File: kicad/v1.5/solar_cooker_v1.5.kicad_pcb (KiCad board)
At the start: 2 copper layers, 88.9 x 99.1 mm, 9 parts, among them U1 microSD, U2 clock_module, U3 anemometer, U4 AM2315, U5 BME680, U6 PT100

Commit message: KiCad update
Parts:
- added D1: LED_GREEN, LED_SMD:LED_1206_3216Metric_Pad1.42x1.75mm_HandSolder, F.Cu at (210.8, 92.5)
- added D2: LED_RED, LED_SMD:LED_1206_3216Metric_Pad1.42x1.75mm_HandSolder, F.Cu at (218.4, 92.5)
- added S1: 500SSP1S2M2QEA, switch:SW_500SSP1S2M2QEA, F.Cu at (215.9, 70.7)
- added U7: pyranometer, custom_components:screw_terminal_4pin, F.Cu at (256.5, 104.1)
- R1: footprint Resistor_SMD:R_0201_0603Metric_Pad0.64x0.40mm_HandSolder -> Resistor_SMD:R_1206_3216Metric
- R2, R3: footprint Resistor_SMD:R_0201_0603Metric_Pad0.64x0.40mm_HandSolder -> Resistor_SMD:R_1206_3216Metric_Pad1.30x1.75mm_HandSolder
- moved R1 30.0 mm to (231.1, 99.1)
- moved R3 16.1 mm to (218.4, 84.0), turned to 90 degrees
- moved U5 15.2 mm to (200.7, 48.3)
- moved R2 14.2 mm to (210.8, 84.0), turned to 90 degrees
- moved U3 2.54 mm to (256.5, 83.8)
- moved U6 2.54 mm to (251.5, 38.1)

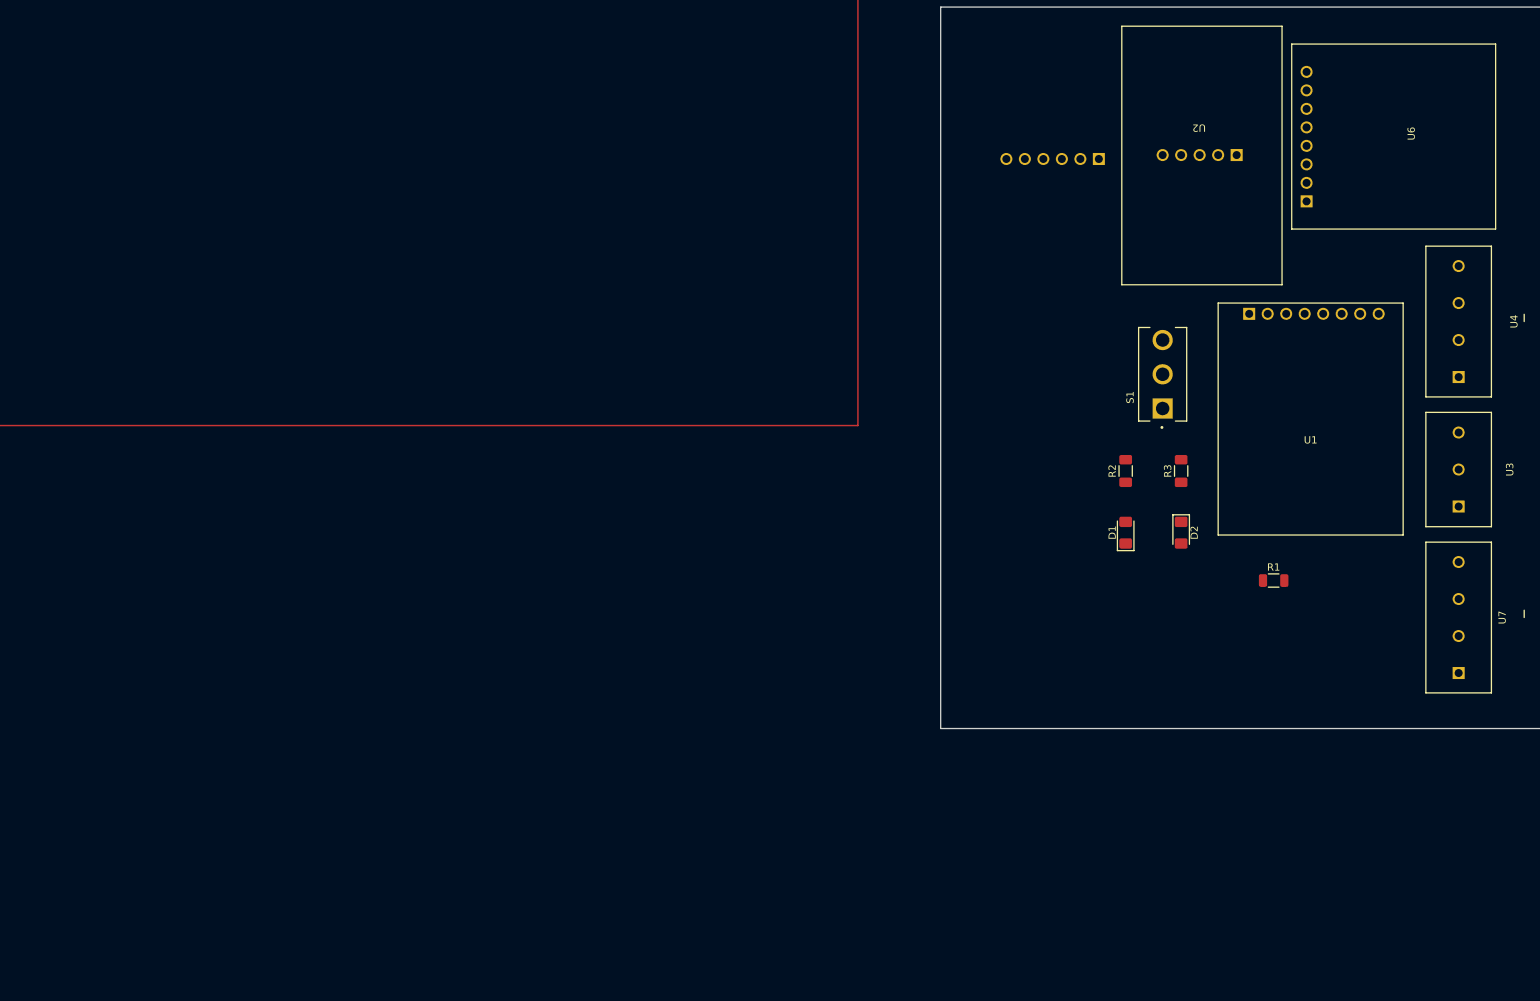
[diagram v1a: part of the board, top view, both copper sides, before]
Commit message: added Arduino Mega KiCad
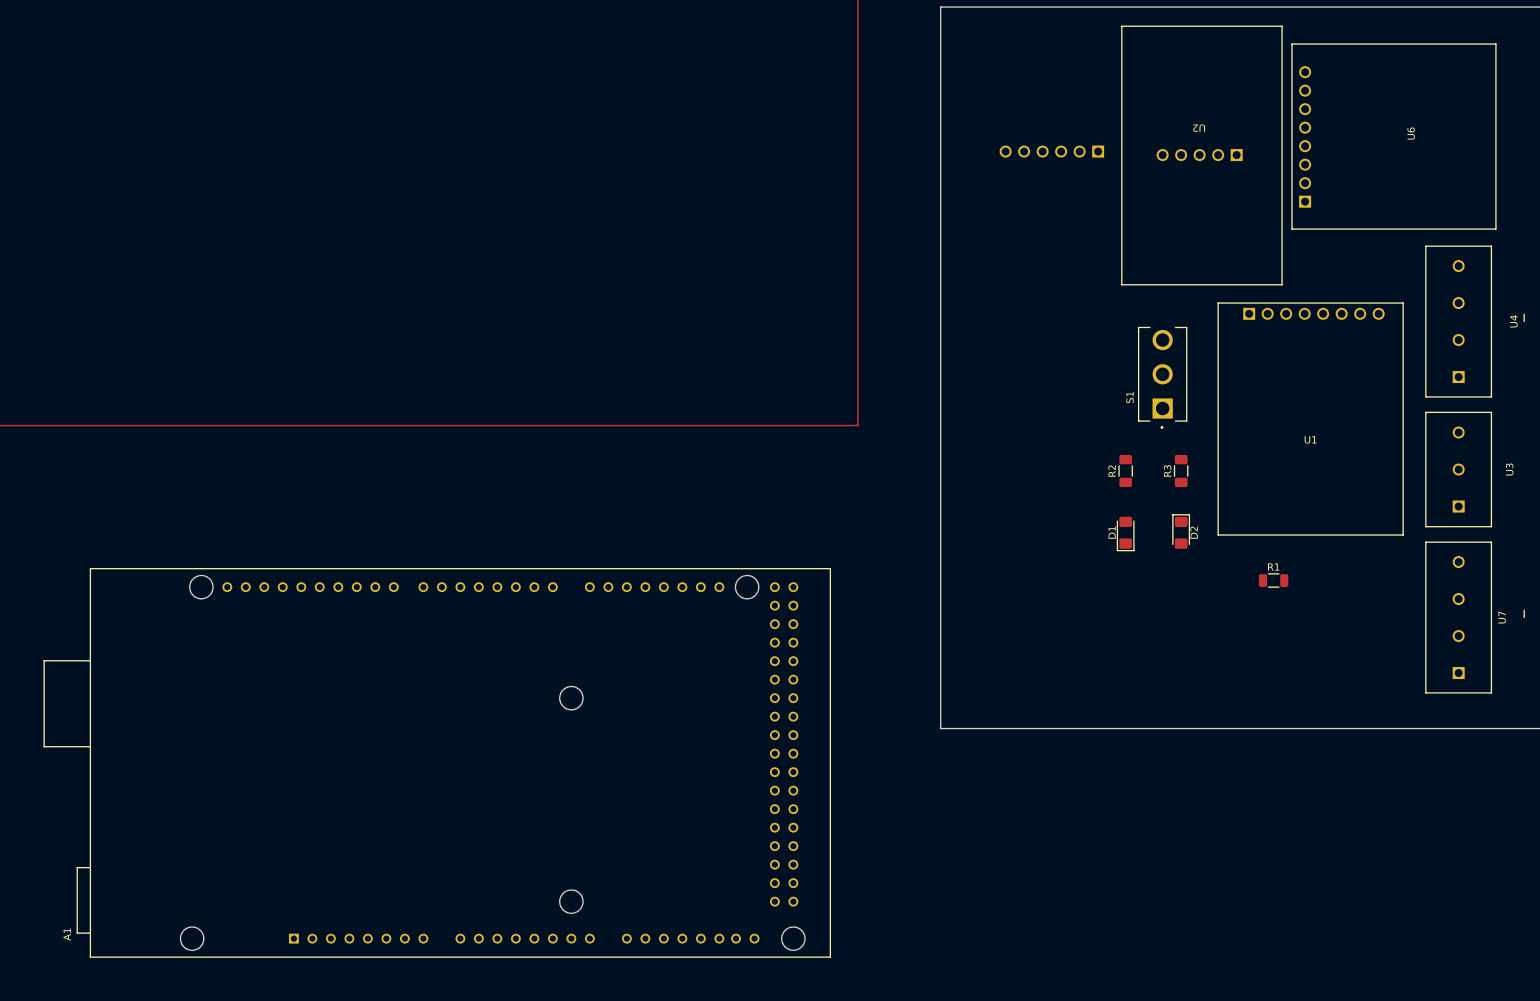
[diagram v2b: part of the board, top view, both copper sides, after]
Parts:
- added A1: A000067, Arduino Mega:ARDUINO_A000067, F.Cu at (119.5, 124.1)

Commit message: pcb has now 3 pt100 sensors
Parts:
- added U8: PT100, custom_components:PT100, F.Cu at (111.8, 147.8)
- added U9: PT100, custom_components:PT100, F.Cu at (80.1, 147.8)
- moved S1 199.1 mm to (33.0, 149.5)
- moved U1 198.6 mm to (43.2, 125.3), turned to -90 degrees
- moved U6 183.6 mm to (80.1, 103.9), turned to 0 degrees
- moved U2 182.9 mm to (46.8, 96.8), turned to 90 degrees
- moved U5 181.1 mm to (50.8, 149.9), turned to 90 degrees
- moved U7 123.1 mm to (142.2, 149.9), turned to 0 degrees
- moved U3 114.9 mm to (162.6, 149.9), turned to 0 degrees
- moved U4 113.5 mm to (182.9, 149.9), turned to 0 degrees
- moved R3 71.5 mm to (209.3, 154.9), turned to 0 degrees
- moved D2 64.9 mm to (200.8, 154.9), turned to 180 degrees
- moved A1 64.4 mm to (182.9, 113.0), turned to -90 degrees
- moved R2 63.3 mm to (209.3, 147.3), turned to 0 degrees
- moved D1 55.7 mm to (200.8, 147.3), turned to 0 degrees
- moved R1 53.4 mm to (218.4, 150.9), turned to -90 degrees
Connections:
- A1 pad 11: unconnected-(A1-Pad11) -> /D11
- A1 pad 20: unconnected-(A1-Pad20) -> /SDA
- A1 pad 21: unconnected-(A1-Pad21) -> /SCL
- A1 pad 22: unconnected-(A1-Pad22) -> /D22
- A1 pad 23: unconnected-(A1-Pad23) -> /D23
- A1 pad 24: unconnected-(A1-Pad24) -> /D24
- A1 pad 3: unconnected-(A1-Pad3) -> /D4
- A1 pad 50: unconnected-(A1-Pad50) -> /MISO
- A1 pad 51: unconnected-(A1-Pad51) -> /MOSI
- A1 pad 52: unconnected-(A1-Pad52) -> /SCK
- A1 pad 5V_1: unconnected-(A1-+5V_1-Pad5V_1) -> +5V
- A1 pad 6: unconnected-(A1-Pad6) -> /D6
- A1 pad AD0: unconnected-(A1-PadAD0) -> /A0
- A1 pad AD10: unconnected-(A1-PadAD10) -> /A10
- A1 pad GND1: unconnected-(A1-PadGND1) -> GND
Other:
- board size 88.9 x 99.1 mm -> 199.8 x 78.7 mm

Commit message: added GPS to pcb
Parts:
- added U10: GPS, custom_components:GPS, F.Cu at (93.8, 105.4)
- U5: moved to F.Cu
- moved S1 97.7 mm to (130.7, 147.5), turned to 180 degrees
- moved R3 94.4 mm to (116.5, 137.4), turned to 180 degrees
- moved R2 94.0 mm to (116.5, 131.9), turned to 180 degrees
- moved R1 90.2 mm to (128.3, 154.9), turned to 0 degrees
- moved U1 80.3 mm to (121.9, 109.2), turned to 180 degrees
- moved D2 80.1 mm to (122.6, 137.4), turned to 0 degrees
- moved D1 79.7 mm to (122.6, 131.9)
- moved U2 64.6 mm to (92.5, 142.5), turned to 0 degrees
- moved U5 63.1 mm to (113.9, 151.0), turned to 0 degrees
- moved U8 58.0 mm to (60.7, 120.3), turned to -90 degrees
- moved U6 22.4 mm to (60.5, 93.0), turned to -90 degrees
- moved U9 19.1 mm to (61.0, 147.6), turned to -90 degrees
- moved U4 11.7 mm to (194.4, 147.5)
- moved U3 11.3 mm to (173.6, 147.5)
- moved U7 10.8 mm to (152.8, 147.5)
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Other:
- board size 199.8 x 78.7 mm -> 155.4 x 77.1 mm
- board text added: "OFF"
- board text added: "ON"
- board text added: "SD card"
- board text added: "bottom of box"
- board text added: "entry cables"
- board text added: "external kabels"
- board text added: "powerbank"
- board text added: "top side of the box"

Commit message: routing update
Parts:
- moved R3 7.82 mm to (108.7, 137.1)
- moved R2 7.81 mm to (108.7, 132.1)
- moved D2 7.81 mm to (114.8, 137.1)
- moved D1 7.80 mm to (114.8, 132.1)
- moved R1 1.53 mm to (126.8, 154.8)
- moved U6 1.35 mm to (61.0, 94.3)
- moved U8 0.56 mm to (61.0, 120.8)
- moved U9 0.28 mm to (61.0, 147.3)
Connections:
- A1 pad 12: unconnected-(A1-Pad12) -> /D12
- A1 pad 13: unconnected-(A1-Pad13) -> /D13
- U6 pad 1: /White -> unconnected-(U6-RDY-Pad1)
- U6 pad 2: /White -> /D11
- U6 pad 3: /Red -> /MOSI
- U6 pad 4: /Red -> /MISO
- U6 pad 5: unconnected-(U6-RDY-Pad5) -> /SCK
- U6 pad 6: /D11 -> unconnected-(U6-3V3-Pad6)
- U6 pad 7: /MOSI -> GND
- U6 pad 8: /MISO -> +5V
- U8 pad 1: /White -> unconnected-(U8-RDY-Pad1)
- U8 pad 2: /White -> /D12
- U8 pad 3: /Red -> /MOSI
- U8 pad 4: /Red -> /MISO
- U8 pad 5: unconnected-(U8-RDY-Pad5) -> /SCK
- U8 pad 6: /D11 -> unconnected-(U8-3V3-Pad6)
- U8 pad 7: /MOSI -> GND
- U8 pad 8: /MISO -> +5V
- U9 pad 1: /White -> unconnected-(U9-RDY-Pad1)
- U9 pad 2: /White -> /D13
- U9 pad 3: /Red -> /MOSI
- U9 pad 4: /Red -> /MISO
- U9 pad 5: unconnected-(U9-RDY-Pad5) -> /SCK
- U9 pad 6: /D11 -> unconnected-(U9-3V3-Pad6)
- U9 pad 7: /MOSI -> GND
- U9 pad 8: /MISO -> +5V
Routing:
- net /SCK: track 0.00 -> 179.0 mm
- net /MISO: track 0.00 -> 157.4 mm
- net /MOSI: track 0.00 -> 155.9 mm
- net /D11: track 0.00 -> 148.1 mm
- net /D13: track 0.00 -> 148.1 mm
- net /D12: track 0.00 -> 140.9 mm
- net /SCL: track 0.00 -> 128.4 mm
- net /D6: track 0.00 -> 92.9 mm, vias 0 -> 1
- net /D4: track 0.00 -> 79.9 mm
- net /A10: track 0.00 -> 67.6 mm
- net +5V: track 0.00 -> 67.2 mm
- net /A0: track 0.00 -> 65.3 mm
- net /SDA: track 0.00 -> 42.9 mm
- net /D24: track 0.00 -> 34.5 mm

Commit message: routing update
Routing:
- net +5V: track 67.2 -> 220.7 mm, vias 0 -> 2
- net /SDA: track 42.9 -> 193.1 mm
- net /D22: track 0.00 -> 41.1 mm
- net /D23: track 0.00 -> 28.9 mm
- net Net-(D2-K): track 0.00 -> 3.08 mm
- net Net-(D1-K): track 0.00 -> 3.08 mm
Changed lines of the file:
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@@
     (effects (font (size 2 2) (thickness 0.3)) (justify left bottom))
   )
+  (segment (start 110.25 132.096429) (end 113.325 132.096429) (width 0.25) (layer "F.Cu") (net 1))
+  (segment (start 110.25 137.096428) (end 113.325 137.096428) (width 0.25) (layer "F.Cu") (net 3))
   (segment (start 186.9 128.3) (end 192.8 134.2) (width 0.25) (layer "F.Cu") (net 5))
   (segment (start 192.8 134.2) (end 192.8 135.7) (width 0.25) (layer "F.Cu") (net 5))
@@
   (segment (start 120.18 114.435933) (end 139.215933 95.4) (width 0.25) (layer "B.Cu") (net 8))
   (segment (start 139.215933 95.4) (end 144.46 95.4) (width 0.25) (layer "B.Cu") (net 8))
+  (segment (start 107.5446 146.4554) (end 106.68 147.32) (width 0.25) (layer "F.Cu") (net 10))
+  (segment (start 75.81 141.396346) (end 76.483654 142.07) (width 0.25) (layer "F.Cu") (net 10))
+  (segment (start 76.96 103.16) (end 75.81 104.31) (width 0.25) (layer "F.Cu") (net 10))
+  (segment (start 77.366346 142.24) (end 78.74 143.613654) (width 0.25) (layer "F.Cu") (net 10))
+  (segment (start 75.81 104.31) (end 75.81 114.896346) (width 0.25) (layer "F.Cu") (net 10))
+  (segment (start 91.3 143.76) (end 92.45 142.61) (width 0.25) (layer "F.Cu") (net 10))
+  (segment (start 83.65 142.07) (end 85.34 143.76) (width 0.25) (layer "F.Cu") (net 10))
+  (segment (start 75.81 114.896346) (end 76.483654 115.57) (width 0.25) (layer "F.Cu") (net 10))
+  (segment (start 76.96 129.66) (end 75.81 130.81) (width 0.25) (layer "F.Cu") (net 10))
+  (segment (start 78.74 127.88) (end 76.96 129.66) (width 0.25) (layer "F.Cu") (net 10))
+  (segment (start 85.34 143.76) (end 91.3 143.76) (width 0.25) (layer "F.Cu") (net 10))
+  (segment (start 106.1296 141.46) (end 107.5446 142.875) (width 0.25) (layer "F.Cu") (net 10))
+  (segment (start 78.74 143.613654) (end 78.74 147.32) (width 0.25) (layer "F.Cu") (net 10))
+  (segment (start 78.74 117.113654) (end 78.74 127.88) (width 0.25) (layer "F.Cu") (net 10))
+  (segment (start 93.6 141.46) (end 106.1296 141.46) (width 0.25) (layer "F.Cu") (net 10))
+  (segment (start 75.81 141.396346) (end 76.653654 142.24) (width 0.25) (layer "F.Cu") (net 10))
+  (segment (start 76.653654 142.24) (end 77.366346 142.24) (width 0.25) (layer "F.Cu") (net 10))
+  (segment (start 75.81 130.81) (end 75.81 141.396346) (width 0.25) (layer "F.Cu") (net 10))
+  (segment (start 92.45 142.61) (end 93.6 141.46) (width 0.25) (layer "F.Cu") (net 10))
+  (segment (start 107.5446 142.875) (end 107.5446 146.4554) (width 0.25) (layer "F.Cu") (net 10))
+  (segment (start 76.483654 142.07) (end 83.65 142.07) (width 0.25) (layer "F.Cu") (net 10))
+  (segment (start 77.196346 115.57) (end 78.74 117.113654) (width 0.25) (layer "F.Cu") (net 10))
+  (segment (start 76.483654 115.57) (end 77.196346 115.57) (width 0.25) (layer "F.Cu") (net 10))
+  (via (at 78.74 147.32) (size 0.8) (drill 0.4) (layers "F.Cu" "B.Cu") (net 10))
+  (via (at 106.68 147.32) (size 0.8) (drill 0.4) (layers "F.Cu" "B.Cu") (net 10))
   (segment (start 186.76 147.5) (end 195.58 138.68) (width 0.25) (layer "B.Cu") (net 10))
+  (segment (start 112.56 125.545) (end 112.56 137.86) (width 0.25) (layer "B.Cu") (net 10))
+  (segment (start 124.061396 141.725) (end 119.768254 141.725) (width 0.25) (layer "B.Cu") (net 10))
   (segment (start 195.58 138.68) (end 195.58 92.54) (width 0.25) (layer "B.Cu") (net 10))
+  (segment (start 78.74 154.38) (end 76.96 156.16) (width 0.25) (layer "B.Cu") (net 10))
+  (segment (start 128.85 146.513604) (end 124.061396 141.725) (width 0.25) (layer "B.Cu") (net 10))
+  (segment (start 128.85 148.313604) (end 128.85 146.513604) (width 0.25) (layer "B.Cu") (net 10))
+  (segment (start 129.786396 149.25) (end 128.85 148.313604) (width 0.25) (layer "B.Cu") (net 10))
+  (segment (start 119.0946 143.111346) (end 114.885946 147.32) (width 0.25) (layer "B.Cu") (net 10))
+  (segment (start 78.74 147.32) (end 78.74 154.38) (width 0.25) (layer "B.Cu") (net 10))
+  (segment (start 119.768254 141.725) (end 119.0946 142.398654) (width 0.25) (layer "B.Cu") (net 10))
+  (segment (start 107.545 142.875) (end 107.5446 142.875) (width 0.25) (layer "B.Cu") (net 10))
   (segment (start 195.58 92.54) (end 201.64 86.48) (width 0.25) (layer "B.Cu") (net 10))
+  (segment (start 112.56 137.86) (end 107.545 142.875) (width 0.25) (layer "B.Cu") (net 10))
+  (segment (start 119.0946 142.398654) (end 119.0946 143.111346) (width 0.25) (layer "B.Cu") (net 10))
+  (segment (start 135.4246 147.5) (end 133.6746 149.25) (width 0.25) (layer "B.Cu") (net 10))
+  (segment (start 111.76 147.32) (end 106.68 147.32) (width 0.25) (layer "B.Cu") (net 10))
+  (segment (start 133.6746 149.25) (end 129.786396 149.25) (width 0.25) (layer "B.Cu") (net 10))
+  (segment (start 114.885946 147.32) (end 111.76 147.32) (width 0.25) (layer "B.Cu") (net 10))
+  (segment (start 153.747604 93.096) (end 159.996 86.847604) (width 0.25) (layer "B.Cu") (net 11))
   (segment (start 178.4 149.6) (end 164.544 135.744) (width 0.25) (layer "B.Cu") (net 11))
+  (segment (start 87.37 142.61) (end 136.884 93.096) (width 0.25) (layer "B.Cu") (net 11))
   (segment (start 164.544 135.744) (end 156.924 135.744) (width 0.25) (layer "B.Cu") (net 11))
+  (segment (start 160.584129 85.476) (end 161.415871 85.476) (width 0.25) (layer "B.Cu") (net 11))
+  (segment (start 161.415871 85.476) (end 162.004 86.064129) (width 0.25) (layer "B.Cu") (net 11))
   (segment (start 156.924 135.744) (end 155.92 134.74) (width 0.25) (layer "B.Cu") (net 11))
+  (segment (start 159.996 86.064129) (end 160.584129 85.476) (width 0.25) (layer "B.Cu") (net 11))
   (segment (start 191.84 147.5) (end 189.74 149.6) (width 0.25) (layer "B.Cu") (net 11))
+  (segment (start 159.996 86.847604) (end 159.996 86.064129) (width 0.25) (layer "B.Cu") (net 11))
   (segment (start 189.74 149.6) (end 178.4 149.6) (width 0.25) (layer "B.Cu") (net 11))
+  (segment (start 136.884 93.096) (end 153.747604 93.096) (width 0.25) (layer "B.Cu") (net 11))
+  (segment (start 162.004 86.064129) (end 162.004 128.656) (width 0.25) (layer "B.Cu") (net 11))
+  (segment (start 162.004 128.656) (end 155.92 134.74) (width 0.25) (layer "B.Cu") (net 11))
   (segment (start 126.6 126.6) (end 131 131) (width 0.25) (layer "F.Cu") (net 12))
   (segment (start 118.9 125) (end 119.7 124.2) (width 0.25) (layer "F.Cu") (net 12))
@@
   (segment (start 142.6 131) (end 144.42 131) (width 0.25) (layer "B.Cu") (net 17))
   (segment (start 144.42 131) (end 145.76 129.66) (width 0.25) (layer "B.Cu") (net 17))
+  (segment (start 115.498928 138.296428) (end 114.3625 137.16) (width 0.25) (layer "F.Cu") (net 18))
+  (segment (start 145.76 132.2) (end 144.224 133.736) (width 0.25) (layer "F.Cu") (net 18))
+  (segment (start 114.3625 137.16) (end 114.3625 134.033929) (width 0.25) (layer "F.Cu") (net 18))
+  (segment (start 144.224 133.736) (end 144.224 135.176) (width 0.25) (layer "F.Cu") (net 18))
+  (segment (start 141.103572 138.296428) (end 115.498928 138.296428) (width 0.25) (layer "F.Cu") (net 18))
+  (segment (start 144.224 135.176) (end 141.103572 138.296428) (width 0.25) (layer "F.Cu") (net 18))
+  (segment (start 114.3625 134.033929) (end 116.3 132.096429) (width 0.25) (layer "F.Cu") (net 18))
+  (segment (start 143.22 132.2) (end 138.323572 137.096428) (width 0.25) (layer "F.Cu") (net 19))
+  (segment (start 138.323572 137.096428) (end 116.3 137.096428) (width 0.25) (layer "F.Cu") (net 19))
   (segment (start 147.6 135.563072) (end 147.595 135.558072) (width 0.25) (layer "B.Cu") (net 20))
   (segment (start 147.595 135.558072) (end 147.595 99.885) (width 0.25) (layer "B.Cu") (net 20))
